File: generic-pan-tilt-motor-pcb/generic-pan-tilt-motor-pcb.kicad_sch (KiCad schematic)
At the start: 30 parts, among them J1 Conn_01x12, J2 Conn_01x04, J3 Conn_01x04, J4 Conn_01x04, J5 Conn_01x08

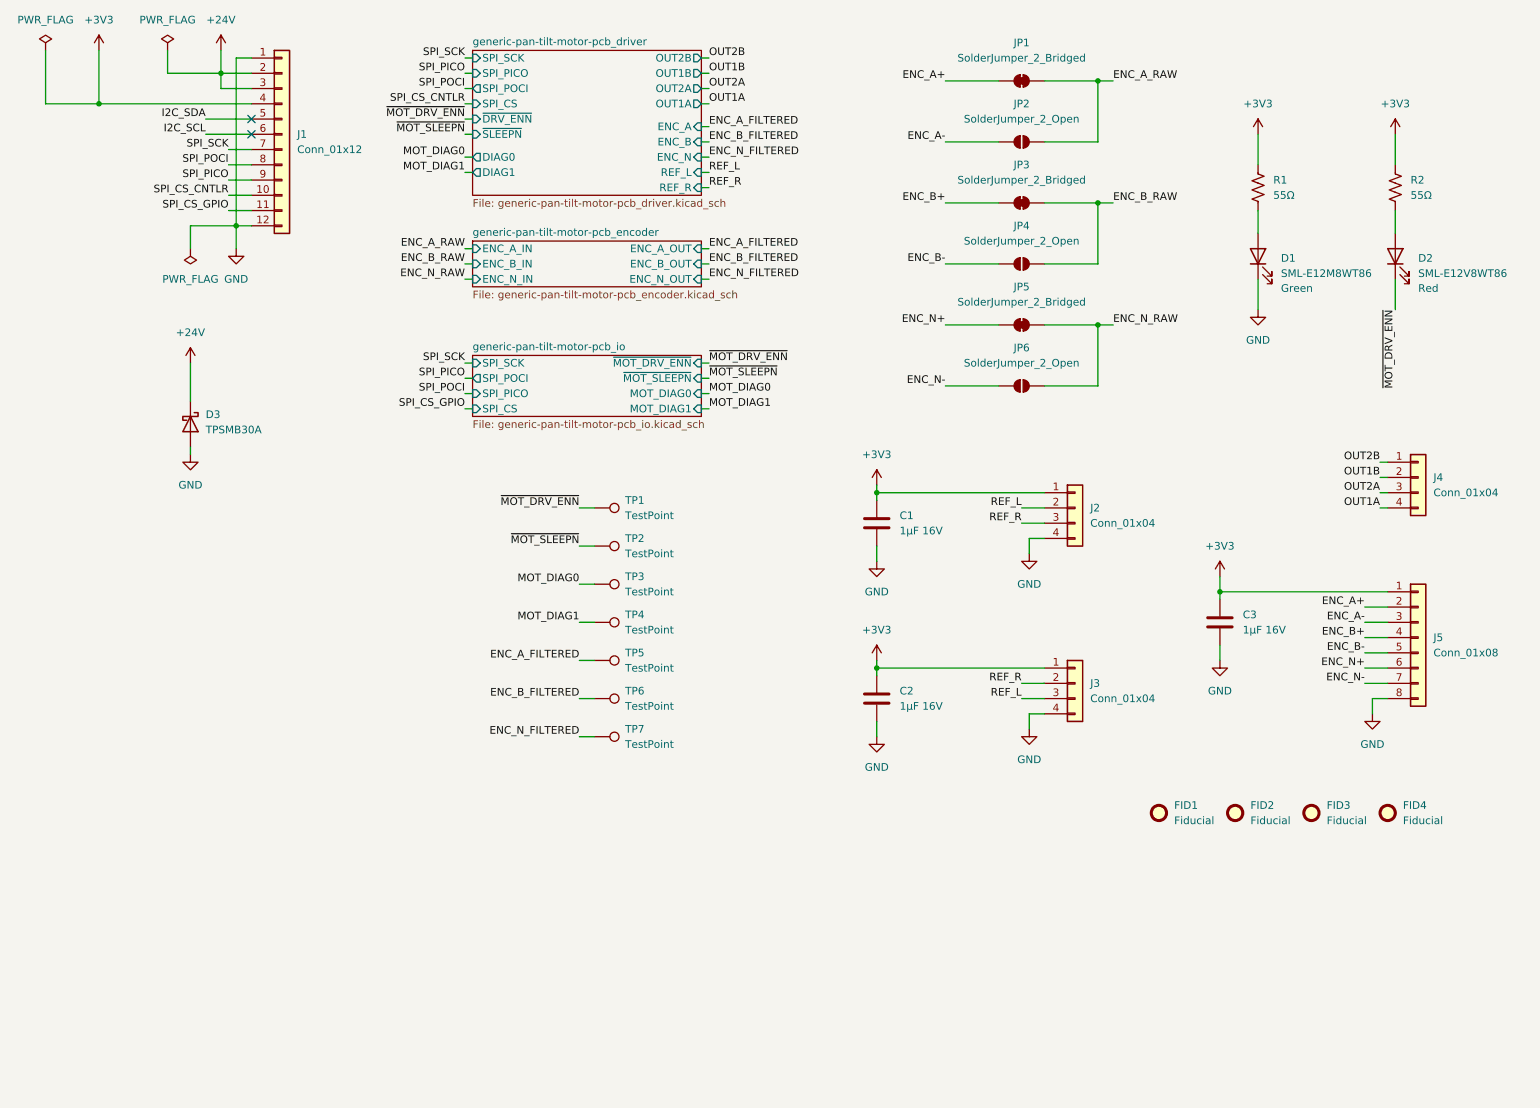
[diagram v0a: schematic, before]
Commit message: motor pcb all footprints, ov circuit
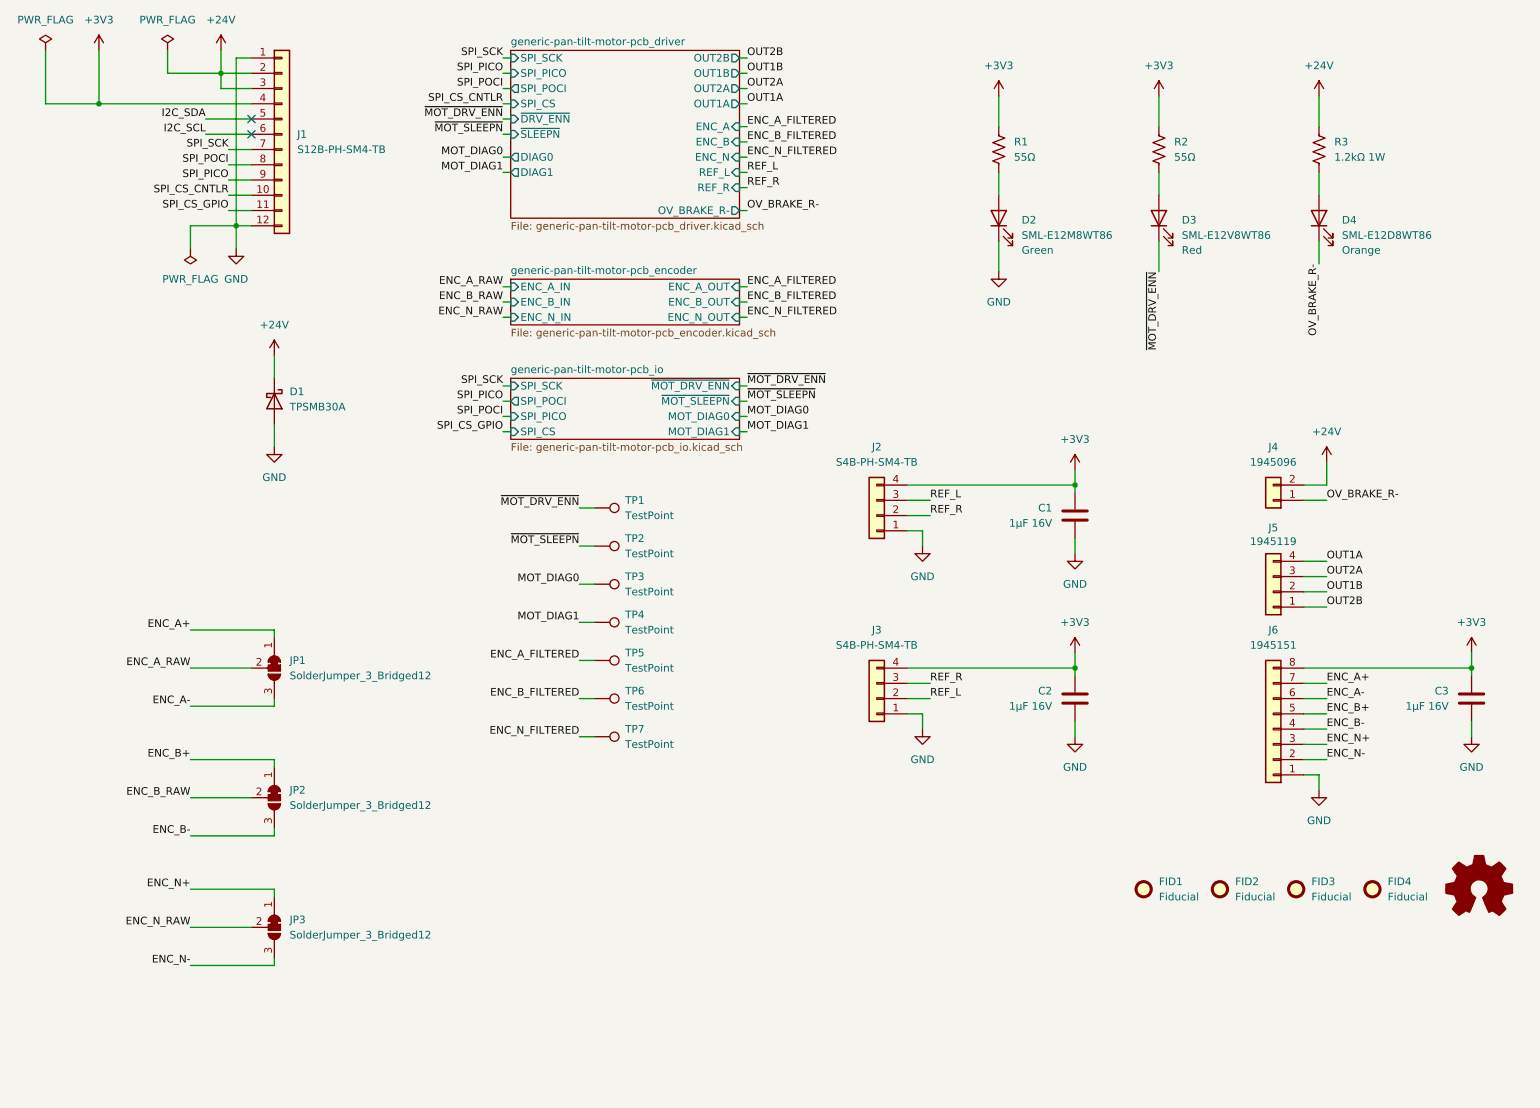
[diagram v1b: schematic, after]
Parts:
- removed J4: Conn_01x04, symbol Connector_Generic:Conn_01x04
- removed JP1, JP3, JP5: SolderJumper_2_Bridged, symbol Jumper:SolderJumper_2_Bridged
- removed JP2, JP4, JP6: SolderJumper_2_Open, symbol Jumper:SolderJumper_2_Open
- added D4: SML-E12D8WT86, LED_SMD:LED_0603_1608Metric, symbol Device:LED
- added J4: 1945096, generic-pan-tilt-motor-pcb:PhoenixContact_PST_1.0_2-3.5_1x02_P3.5mm_Vertical, symbol Connector_Generic:Conn_01x02
- added J5: 1945119, generic-pan-tilt-motor-pcb:PhoenixContact_PST_1.0_4-3.5_1x04_P3.5mm_Vertical, symbol Connector_Generic:Conn_01x04
- added JP1, JP2, JP3: SolderJumper_3_Bridged12, Jumper:SolderJumper-3_P1.3mm_Bridged12_RoundedPad1.0x1.5mm_NumberLabels, symbol Jumper:SolderJumper_3_Bridged12
- added R3: 1.2kΩ 1W, Resistor_SMD:R_2512_6332Metric, symbol Device:R_US
- added SYM1: Logo_Open_Hardware_Small, Symbol:OSHW-Logo2_7.3x6mm_SilkScreen, symbol Graphic:Logo_Open_Hardware_Small
- C1, C2, C3: footprint (none) -> Capacitor_SMD:C_0603_1608Metric
- D1: renamed from D3; footprint (none) -> Diode_SMD:D_SMB; digikey# (none) -> F6320CT-ND; manf# (none) -> TPSMB30A; mouser# (none) -> 576-TPSMB30A
- D2: renamed from D1; digikey# (none) -> 846-SML-E12M8WT86CT-ND; manf# (none) -> SML-E12M8WT86; mouser# (none) -> 755-SML-E12M8WT86
- D3: renamed from D2; footprint (none) -> LED_SMD:LED_0603_1608Metric; digikey# (none) -> 846-SML-E12V8WT86CT-ND; manf# (none) -> SML-E12V8WT86; mouser# (none) -> 755-SML-E12V8WT86
- FID1, FID2, FID3, FID4: footprint (none) -> Fiducial:Fiducial_0.5mm_Mask1mm
- J1: value Conn_01x12 -> S12B-PH-SM4-TB; footprint (none) -> Connector_JST:JST_PH_S12B-PH-SM4-TB_1x12-1MP_P2.00mm_Horizontal; digikey# (none) -> 455-S12B-PH-SM4-TBCT-ND; manf# (none) -> S12B-PH-SM4-TB
- J2, J3: value Conn_01x04 -> S4B-PH-SM4-TB; footprint (none) -> Connector_JST:JST_PH_S4B-PH-SM4-TB_1x04-1MP_P2.00mm_Horizontal; digikey# (none) -> 455-S4B-PH-SM4-TBCT-ND; manf# (none) -> S4B-PH-SM4-TB
- J6: renamed from J5; value Conn_01x08 -> 1945151; footprint (none) -> generic-pan-tilt-motor-pcb:PhoenixContact_PST_1.0_8-3.5_1x08_P3.5mm_Vertical; digikey# (none) -> 277-1755-ND; manf# (none) -> 1945151; mouser# (none) -> 651-1945151
- R1, R2: footprint (none) -> Resistor_SMD:R_0402_1005Metric
- TP1, TP2, TP3, TP4, TP5, TP6, TP7: footprint (none) -> TestPoint:TestPoint_Pad_1.0x1.0mm
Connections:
- net +24V: now also J4.2 (Pin_2), R3.1
- net +3V3: now also J2.4 (Pin_4), J3.4 (Pin_4), J6.8 (Pin_8); no longer J2.1 (Pin_1), J3.1 (Pin_1), J6.1 (Pin_1)
- net ENC_A+: now also J6.7 (Pin_7), JP1.1 (A); no longer J6.2 (Pin_2)
- net ENC_A-: now also J6.6 (Pin_6), JP1.3 (B); no longer J6.3 (Pin_3)
- net ENC_A_RAW: now also JP1.2 (C)
- net ENC_B+: now also J6.5 (Pin_5), JP2.1 (A); no longer J6.4 (Pin_4)
- net ENC_B-: now also J6.4 (Pin_4), JP2.3 (B); no longer J6.5 (Pin_5)
- net ENC_B_RAW: now also JP2.2 (C)
- net ENC_N+: now also J6.3 (Pin_3), JP3.1 (A); no longer J6.6 (Pin_6)
- net ENC_N-: now also J6.2 (Pin_2), JP3.3 (B); no longer J6.7 (Pin_7)
- net ENC_N_RAW: now also JP3.2 (C)
- net GND: now also J2.1 (Pin_1), J3.1 (Pin_1), J6.1 (Pin_1); no longer J2.4 (Pin_4), J3.4 (Pin_4), J6.8 (Pin_8)
- net OUT1A: now also J5.4 (Pin_4)
- net OUT1B: now also J5.2 (Pin_2)
- net OUT2A: now also J5.3 (Pin_3)
- net OUT2B: now also J5.1 (Pin_1)
- net REF_L: now also J2.3 (Pin_3), J3.2 (Pin_2); no longer J2.2 (Pin_2), J3.3 (Pin_3)
- net REF_R: now also J2.2 (Pin_2), J3.3 (Pin_3); no longer J2.3 (Pin_3), J3.2 (Pin_2)
- new net: D4.2 (A), R3.2
- new net OV_BRAKE_R-: D4.1 (K), J4.1 (Pin_1)
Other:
- sheet generic-pan-tilt-motor-pcb_driver ports: added OV_BRAKE_R-; removed none
- moved on the sheet: C1, C2, C3, D1, D2, D3, FID1, FID2, FID3, FID4, J2, J6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

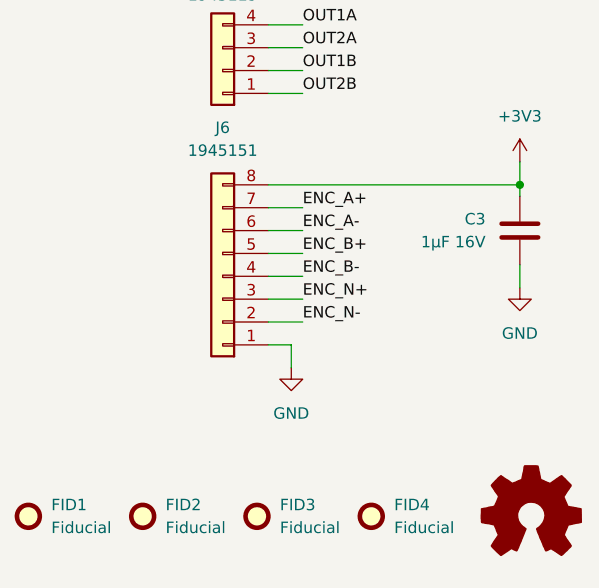
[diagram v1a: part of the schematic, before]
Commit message: motor reorder enc connector
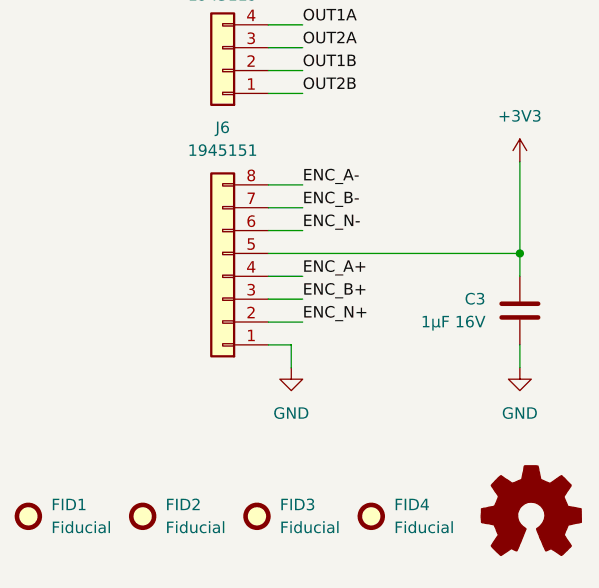
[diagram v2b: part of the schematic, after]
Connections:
- net +3V3: now also J6.5 (Pin_5); no longer J6.8 (Pin_8)
- net ENC_A+: now also J6.4 (Pin_4); no longer J6.7 (Pin_7)
- net ENC_A-: now also J6.8 (Pin_8); no longer J6.6 (Pin_6)
- net ENC_B+: now also J6.3 (Pin_3); no longer J6.5 (Pin_5)
- net ENC_B-: now also J6.7 (Pin_7); no longer J6.4 (Pin_4)
- net ENC_N+: now also J6.2 (Pin_2); no longer J6.3 (Pin_3)
- net ENC_N-: now also J6.6 (Pin_6); no longer J6.2 (Pin_2)
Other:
- moved on the sheet: C3
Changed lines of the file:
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@@
+	)
+	(junction
+		(at 257.81 135.89)
+		(diameter 0)
+		(color 0 0 0 0)
 	)
 	(junction
@@
 		(color 0 0 0 0)
 	)
-	(junction
-		(at 257.81 128.27)
-		(diameter 0)
-		(color 0 0 0 0)
-	)
 	(no_connect
 		(at 54.61 39.37)
@@
 	(wire
 		(pts
-			(xy 257.81 129.54) (xy 257.81 128.27)
+			(xy 257.81 138.43) (xy 257.81 135.89)
 		)
 		(stroke
@@
 	(wire
 		(pts
-			(xy 257.81 128.27) (xy 229.87 128.27)
+			(xy 257.81 135.89) (xy 229.87 135.89)
 		)
 		(stroke
@@
 	(wire
 		(pts
-			(xy 233.68 135.89) (xy 229.87 135.89)
+			(xy 233.68 128.27) (xy 229.87 128.27)
 		)
 		(stroke
@@
 	(wire
 		(pts
-			(xy 257.81 137.16) (xy 257.81 139.7)
+			(xy 257.81 146.05) (xy 257.81 148.59)
 		)
 		(stroke
@@
 	(wire
 		(pts
-			(xy 257.81 125.73) (xy 257.81 128.27)
-		)
-		(stroke
-			(width 0)
-			(type default)
-		)
-	)
-	(wire
-		(pts
 			(xy 167.64 130.81) (xy 163.83 130.81)
 		)
@@
 		(pts
 			(xy 96.52 88.9) (xy 97.79 88.9)
+		)
+		(stroke
+			(width 0)
+			(type default)
+		)
+	)
+	(wire
+		(pts
+			(xy 257.81 125.73) (xy 257.81 135.89)
 		)
 		(stroke
@@
 	)
 	(label "ENC_B-"
-		(at 233.68 138.43 0)
+		(at 233.68 130.81 0)
 		(fields_autoplaced yes)
 		(effects
@@
 	)
 	(label "ENC_N-"
-		(at 233.68 143.51 0)
+		(at 233.68 133.35 0)
 		(fields_autoplaced yes)
 		(effects
@@
 	)
 	(label "ENC_A-"
-		(at 233.68 133.35 0)
+		(at 233.68 128.27 0)
 		(fields_autoplaced yes)
 		(effects
@@
 	)
 	(label "ENC_B+"
-		(at 233.68 135.89 0)
+		(at 233.68 140.97 0)
 		(fields_autoplaced yes)
 		(effects
@@
 	)
 	(label "ENC_A+"
-		(at 233.68 130.81 0)
+		(at 233.68 138.43 0)
 		(fields_autoplaced yes)
 		(effects
@@
 	)
 	(label "ENC_N+"
-		(at 233.68 140.97 0)
+		(at 233.68 143.51 0)
 		(fields_autoplaced yes)
 		(effects
@@
 	(symbol
 		(lib_id "Device:C")
-		(at 257.81 133.35 0)
+		(at 257.81 142.24 0)
 		(mirror y)
 		(unit 1)
@@
 		(dnp no)
 		(property "Reference" "C3"
-			(at 254 132.0799 0)
+			(at 254 140.9699 0)
 			(effects
 				(font
@@
 		)
 		(property "Value" "1µF 16V"
-			(at 254 134.6199 0)
+			(at 254 143.5099 0)
 			(effects
 				(font
@@
 		)
 		(property "Footprint" "Capacitor_SMD:C_0603_1608Metric"
-			(at 256.8448 137.16 0)
+			(at 256.8448 146.05 0)
 			(effects
 				(font
@@
 		)
 		(property "Datasheet" "~"
-			(at 257.81 133.35 0)
+			(at 257.81 142.24 0)
 			(effects
 				(font
@@
 		)
 		(property "Description" "Unpolarized capacitor"
-			(at 257.81 133.35 0)
+			(at 257.81 142.24 0)
 			(effects
 				(font
@@
 	(symbol
 		(lib_id "power:GND")
-		(at 257.81 139.7 0)
+		(at 257.81 148.59 0)
 		(mirror y)
 		(unit 1)
@@
 		(fields_autoplaced yes)
 		(property "Reference" "#PWR019"
-			(at 257.81 146.05 0)
+			(at 257.81 154.94 0)
 			(effects
 				(font
@@
 		)
 		(property "Value" "GND"
-			(at 257.81 144.78 0)
+			(at 257.81 153.67 0)
 			(effects
 				(font
@@
 		)
 		(property "Footprint" ""
-			(at 257.81 139.7 0)
+			(at 257.81 148.59 0)
 			(effects
 				(font
@@
 		)
 		(property "Datasheet" ""
-			(at 257.81 139.7 0)
+			(at 257.81 148.59 0)
 			(effects
 				(font
@@
 		)
 		(property "Description" "Power symbol creates a global label with name \"GND\" , ground"
-			(at 257.81 139.7 0)
-			(effects
-				(font
+			(at 257.81 148.59 0)
+			(effects
+				(font

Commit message: motor basic layout
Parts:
- added H1, H2, H3, H4: MountingHole, MountingHole:MountingHole_3.2mm_M3, symbol Mechanical:MountingHole
- J1: value S12B-PH-SM4-TB -> B12B-PH-SM4-TBT; footprint Connector_JST:JST_PH_S12B-PH-SM4-TB_1x12-1MP_P2.00mm_Horizontal -> Connector_JST:JST_PH_B12B-PH-SM4-TB_1x12-1MP_P2.00mm_Vertical
- J2, J3: footprint Connector_JST:JST_PH_S4B-PH-SM4-TB_1x04-1MP_P2.00mm_Horizontal -> Connector_JST:JST_PH_B4B-PH-SM4-TB_1x04-1MP_P2.00mm_Vertical
